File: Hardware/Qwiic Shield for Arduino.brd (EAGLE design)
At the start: 53.3 x 59.7 mm, 25 parts, among them J1 Qwiic Right Angle, J10 Qwiic Right Angle, J8 Qwiic Right Angle, J9 Qwiic Right Angle, Q1 BSS138, Q2 BSS138, U1 ARDUINO UNO

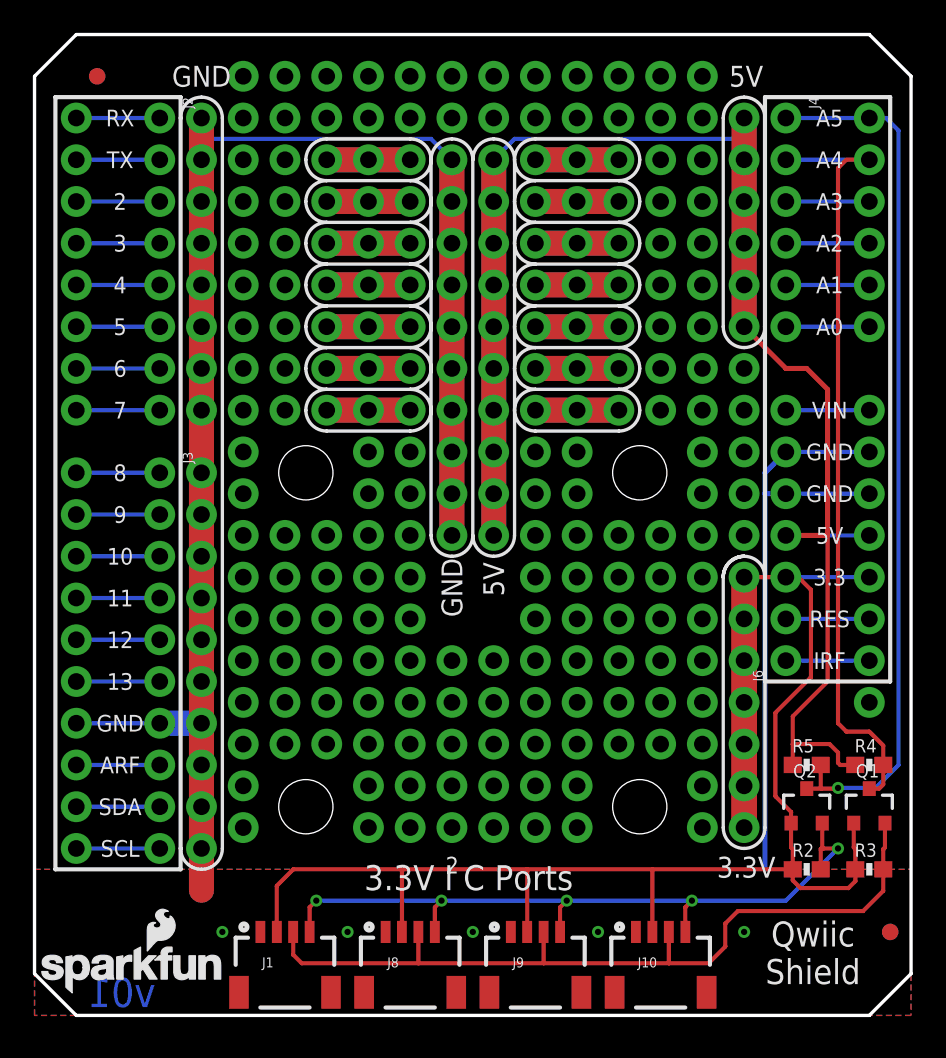
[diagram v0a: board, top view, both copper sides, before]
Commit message: Added notch for barrel jack
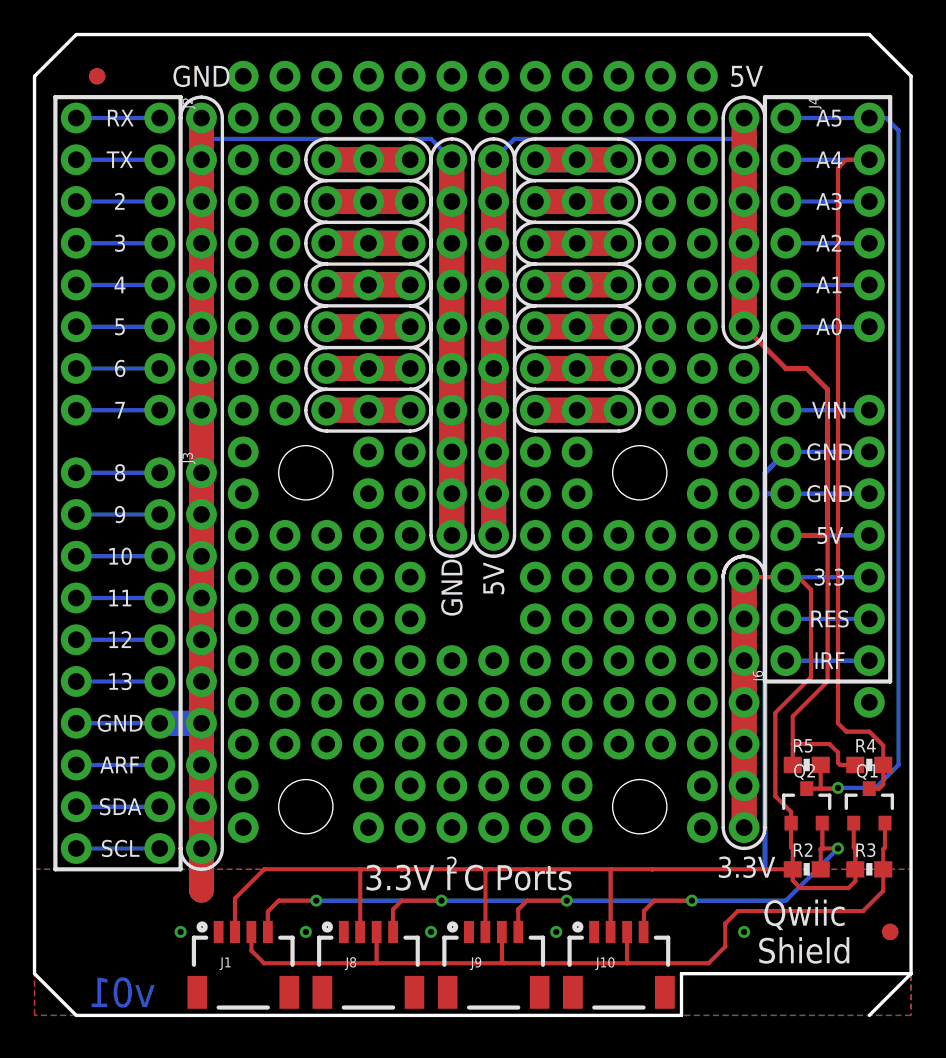
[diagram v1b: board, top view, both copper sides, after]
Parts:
- removed U$1: (no value), SparkFun-Aesthetics:SFE_LOGO_NAME_FLAME_.1
- moved J1 2.54 mm to (12.7, 5.08)
- moved J10 2.54 mm to (35.6, 5.08)
- moved J8 2.54 mm to (20.3, 5.08)
- moved J9 2.54 mm to (27.9, 5.08)
- moved LOGO1 1.27 mm to (47.0, 8.89)
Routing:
- net 3.3V: track 128.0 -> 115.0 mm
- net SCL: track 45.2 -> 54.9 mm
- net SDA: track 50.0 -> 52.5 mm
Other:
- outline, holes or cut-outs redrawn

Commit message: Post Design review changes
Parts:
- added U$1: (no value), SparkFun-Aesthetics:SFE_LOGO_FLAME_.2
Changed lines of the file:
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@@
 <element name="FD3" library="SparkFun-Aesthetics" package="FIDUCIAL-1X2" value="FIDUCIAL1X2" x="52.07" y="5.08" rot="MR0"/>
 <element name="FD4" library="SparkFun-Aesthetics" package="FIDUCIAL-1X2" value="FIDUCIAL1X2" x="3.81" y="57.15" rot="MR0"/>
+<element name="U$1" library="SparkFun-Aesthetics" package="SFE_LOGO_FLAME_.2" value="" x="3.1496" y="2.2987"/>
 </elements>
 <signals>

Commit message: Changed version number
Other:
- board text added: "v10"
- board text removed: "v01"
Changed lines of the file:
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@@
 <text x="46.609" y="5.08" size="1.524" layer="22" font="vector" ratio="15" rot="MR0" align="center">Qwiic
 Shield</text>
-<text x="7.366" y="0.508" size="1.778" layer="16" font="vector" ratio="15" rot="MR0">v01</text>
+<text x="7.366" y="0.508" size="1.778" layer="16" font="vector" ratio="15" rot="MR0">v10</text>
 <text x="21.59" y="-30.48" size="1.778" layer="51">A. England</text>
 <dimension x1="0" y1="0" x2="0" y2="59.69" x3="-6.35" y3="29.845" textsize="1.778" layer="47"/>
